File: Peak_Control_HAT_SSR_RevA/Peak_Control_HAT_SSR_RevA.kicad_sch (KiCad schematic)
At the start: 27 parts, among them J1 Raspberry Pi 40-Pin GPIO Head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, J11 I2C_EXPANSION, J2 24V_IN, J3 PROJECTOR_SW24V_GND, J4 VIEWER_SW24V_GND, J5 AUX1_SW24V_GND, J6 AUX2_SW24V_GND, U1 G3VM-61GR2, U2 G3VM-61GR2, U3 G3VM-61GR2, U4 G3VM-61GR2

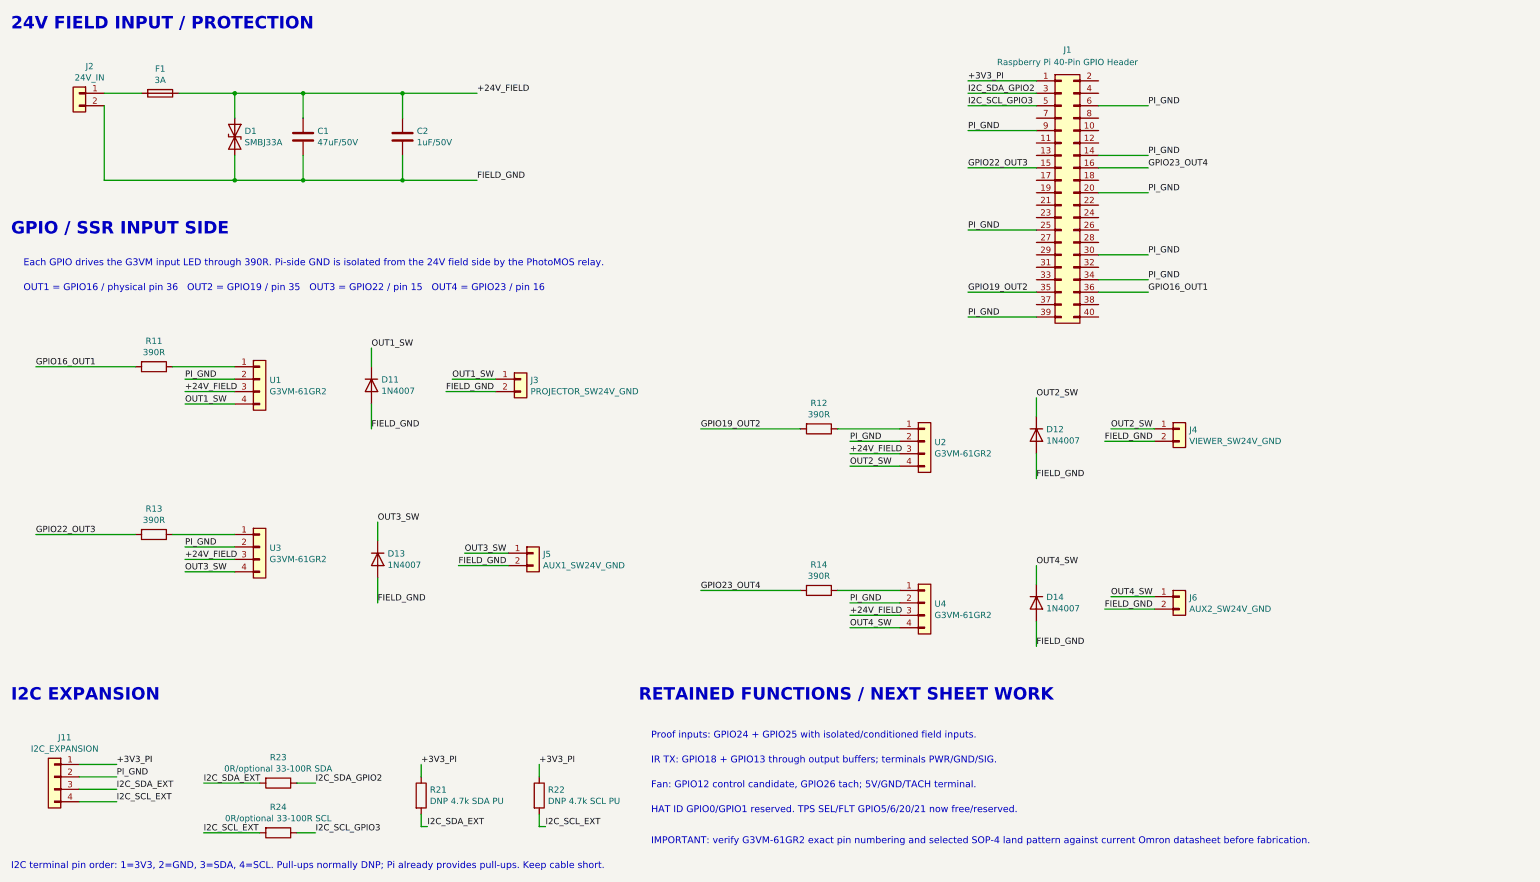
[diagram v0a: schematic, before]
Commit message: Finalized Rev A component placement before routing
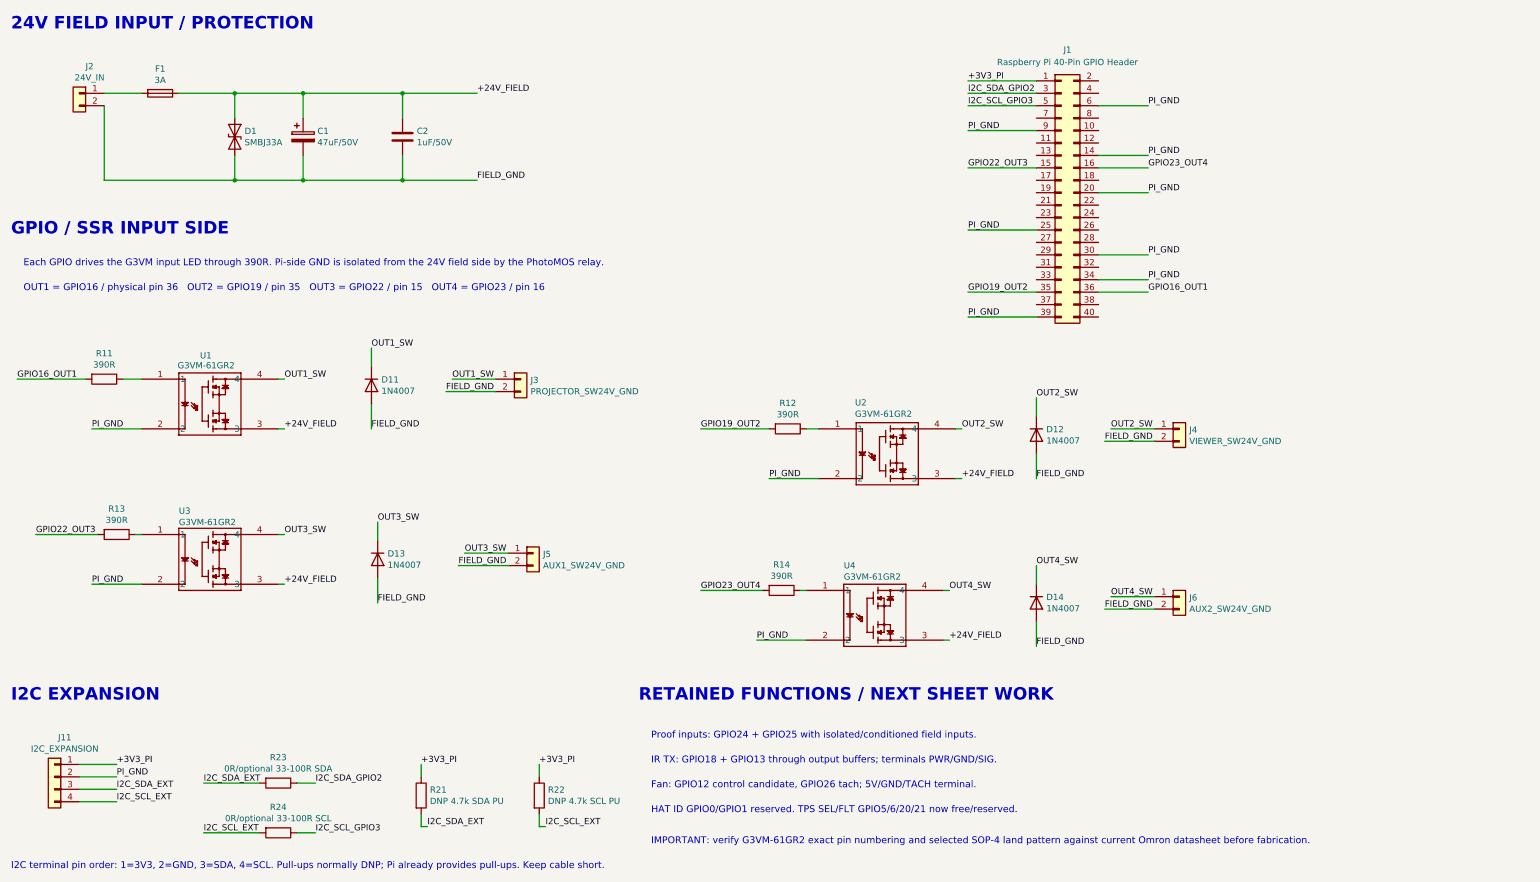
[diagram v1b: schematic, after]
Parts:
- C1: footprint (none) -> Capacitor_THT:CP_Radial_D8.0mm_P3.50mm; symbol Device:C -> Device:C_Polarized
- C2: footprint (none) -> Capacitor_SMD:C_0805_2012Metric_Pad1.18x1.45mm_HandSolder
- D1: footprint (none) -> Diode_SMD:D_SMB_Handsoldering
- D11, D12, D13, D14: footprint (none) -> Diode_THT:D_DO-41_SOD81_P10.16mm_Horizontal
- F1: footprint (none) -> Fuse:Fuseholder_Clip-5x20mm_Bel_FC-203-22_Lateral_P17.80x5.00mm_D1.17mm_Horizontal
- J1: footprint (none) -> Connector_PinSocket_2.54mm:PinSocket_2x20_P2.54mm_Vertical
- J11: footprint (none) -> TerminalBlock_Phoenix:TerminalBlock_Phoenix_MKDS-1,5-4-5.08_1x04_P5.08mm_Horizontal
- J2, J3, J4, J5, J6: footprint (none) -> TerminalBlock_Phoenix:TerminalBlock_Phoenix_MKDS-1,5-2-5.08_1x02_P5.08mm_Horizontal
- R11, R12, R13, R14, R21, R22, R23, R24: footprint (none) -> Resistor_SMD:R_0805_2012Metric_Pad1.20x1.40mm_HandSolder
- U1, U2, U3, U4: footprint (none) -> Omron:G-SOP4_OMR; symbol Connector_Generic:Conn_01x04 -> Omron_G3VM:G3VM-61GR2
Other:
- moved on the sheet: R11, R12, R13, R14

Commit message: Added most traces and zones
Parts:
- added C31: 22uF 50V, Capacitor_THT:CP_Radial_D5.0mm_P2.00mm, symbol Device:C_Polarized
- added C32: 47uF 16V, Capacitor_THT:CP_Radial_D5.0mm_P2.00mm, symbol Device:C_Polarized
- added J12: Fan 5V, Connector_JST:JST_XH_B2B-XH-A_1x02_P2.50mm_Vertical, symbol Connector_Generic:Conn_01x02
- added U5: OKI-78SR-5_1.5-W36-C, Converter_DCDC:Converter_DCDC_Murata_OKI-78SR_Vertical, symbol Converter_DCDC:OKI-78SR-5_1.5-W36-C
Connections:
- net +24V_FIELD: now also C31.1, U5.1 (IN)
- net FIELD_GND: now also C31.2, C32.2, J12.2 (Pin_2), U5.2 (GND)
- new net +5V_FAN: C32.1, J12.1 (Pin_1), U5.3 (OUT)
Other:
- moved on the sheet: J1

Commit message: Added pulldown resistors for SSRs
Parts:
- added R15, R16, R17, R18: 100K, Resistor_SMD:R_0805_2012Metric_Pad1.20x1.40mm_HandSolder, symbol Device:R
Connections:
- net GPIO16_OUT1: now also R15.1
- net GPIO19_OUT2: now also R16.1
- net GPIO22_OUT3: now also R17.1
- net GPIO23_OUT4: now also R18.1
- net PI_GND: now also R15.2, R16.2, R17.2, R18.2

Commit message: Passed ERC checks, needs final pre-fab review
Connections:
- no-connect marks 0 -> 25

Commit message: Created Peak_Control_SSR_Interface project for V1
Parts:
- added J21: POR1, TerminalBlock_Phoenix:TerminalBlock_Phoenix_MKDS-1,5-2-5.08_1x02_P5.08mm_Horizontal, symbol Connector_Generic:Conn_01x02
- added J22: POR2, TerminalBlock_Phoenix:TerminalBlock_Phoenix_MKDS-1,5-2-5.08_1x02_P5.08mm_Horizontal, symbol Connector_Generic:Conn_01x02
- added J23: IR1, TerminalBlock_Phoenix:TerminalBlock_Phoenix_MKDS-1,5-2-5.08_1x02_P5.08mm_Horizontal, symbol Connector_Generic:Conn_01x02
- added J24: IR2, TerminalBlock_Phoenix:TerminalBlock_Phoenix_MKDS-1,5-2-5.08_1x02_P5.08mm_Horizontal, symbol Connector_Generic:Conn_01x02
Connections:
- net PI_GND: now also J21.2 (Pin_2), J22.2 (Pin_2), J23.2 (Pin_2), J24.2 (Pin_2)
- net GPIO17_IR1: now reaches J1.11 (Pin_11)
- net GPIO17_IR1: now also J23.1 (Pin_1)
- net GPIO18_IR2: now reaches J1.12 (Pin_12)
- net GPIO18_IR2: now also J24.1 (Pin_1)
- net GPIO24_POR1: now reaches J1.18 (Pin_18)
- net GPIO24_POR1: now also J21.1 (Pin_1)
- net GPIO25_POR2: now reaches J1.22 (Pin_22)
- net GPIO25_POR2: now also J22.1 (Pin_1)
- no-connect marks 25 -> 21
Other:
- note added: "24V-5V 2-WIRE FAN CIRCUIT"
